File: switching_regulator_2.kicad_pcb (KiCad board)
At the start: 2 copper layers, 57.5 x 54 mm, 11 parts, among them IC1 ST1S41PHR, J1 TBL009-254-04GY-2GY, J2 TBL009-254-04GY-2GY, J3 571-0100, J4 571-0500

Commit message: [ADD] logos
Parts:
- added G***: LOGO, logos:irregular_lines_logo, F.Cu at (76.6, 49.9)
- added G***: LOGO, logos:irregular_lines_logo, B.Cu at (76.7, 49.8)
- added Output    V: LOGO, logos:pulga_logo, F.Cu at (59.3, 35.3)
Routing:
- net /Vout: track 23.1 -> 23.8 mm
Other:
- board size 57.5 x 54 mm -> 53.5 x 54 mm

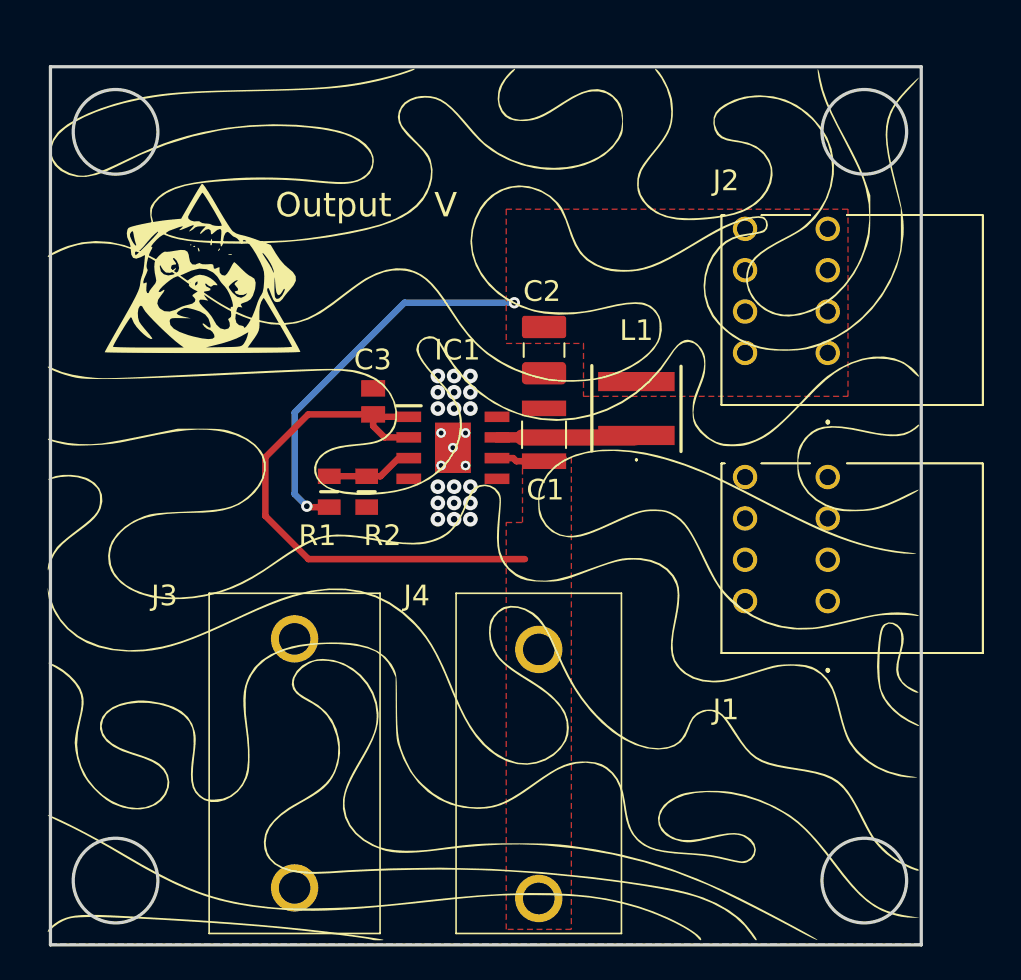
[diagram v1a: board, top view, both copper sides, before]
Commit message: [ADD] curved tracks
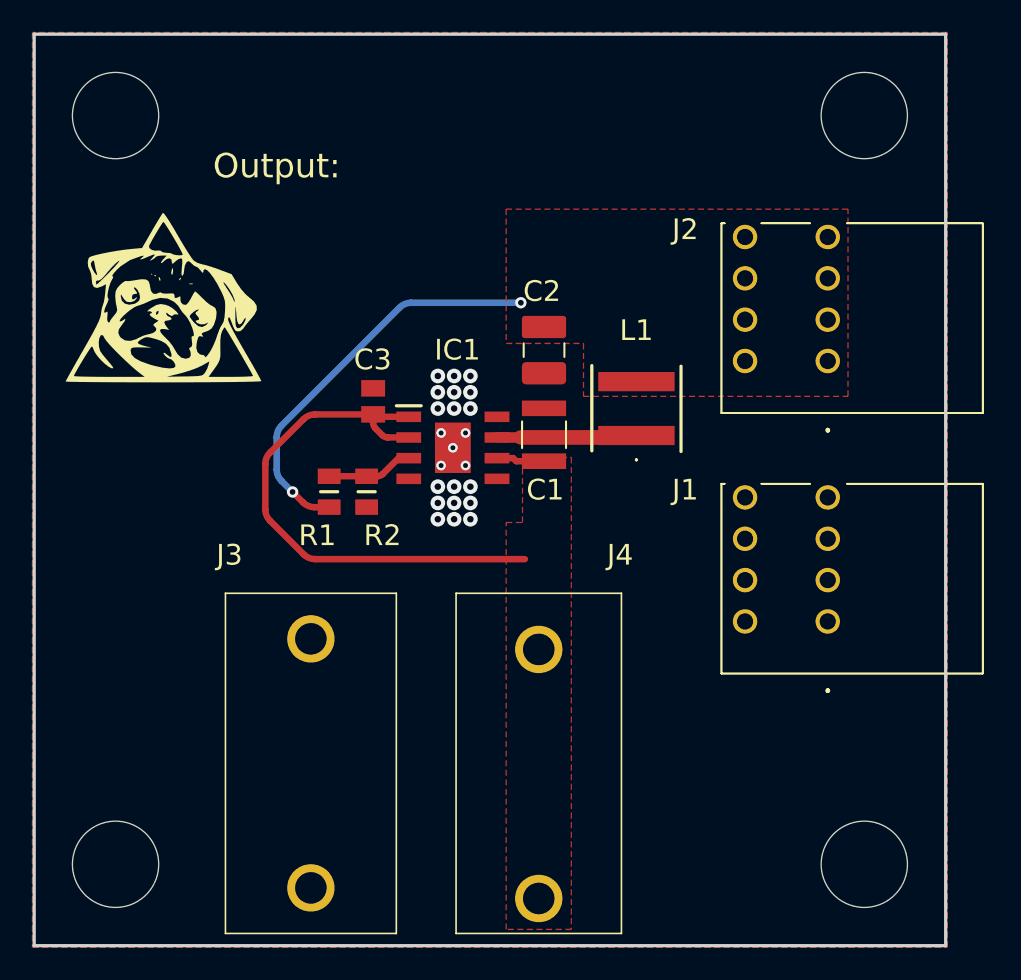
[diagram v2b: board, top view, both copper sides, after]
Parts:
- removed G*** (x2): LOGO, logos:irregular_lines_logo
- added REF**: MountingHole_5.3mm_M5_ISO14580, MountingHole:MountingHole_5.3mm_M5_ISO14580, F.Cu at (54.0, 26.0)
- added REF**: MountingHole_5.3mm_M5_ISO14580, MountingHole:MountingHole_5.3mm_M5_ISO14580, F.Cu at (100.0, 26.0)
- added REF**: MountingHole_5.3mm_M5_ISO14580, MountingHole:MountingHole_5.3mm_M5_ISO14580, F.Cu at (54.0, 72.0)
- added REF**: MountingHole_5.3mm_M5_ISO14580, MountingHole:MountingHole_5.3mm_M5_ISO14580, F.Cu at (100.0, 72.0)
- Output:: renamed from Output    V
- moved Output: 3.00 mm to (56.9, 37.1)
- moved J1 1.25 mm to (97.8, 57.1)
- moved J3 1.00 mm to (66.0, 58.1)
- moved J2 0.50 mm to (97.8, 41.1)
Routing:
- net /Vout: track 23.8 -> 24.9 mm
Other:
- board size 53.5 x 54 mm -> 56 x 56 mm
